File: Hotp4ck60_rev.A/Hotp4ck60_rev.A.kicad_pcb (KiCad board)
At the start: 2 copper layers, 284.7 x 94.2 mm, 43 parts, among them Q1 2N7002, SW1 PWR, U1 nRF52840, U2 BQ24075RGT, U3 TPS7A20xxxDQN, U4 MAX17048, X1 32 MHz, X2 32.768 KHz

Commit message: 기판 아트웍 재시작
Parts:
- removed the REF** at (0.00, 0.00)
- added REF**: hotp4ck60, lib:Neo60-2, F.Cu at (0.00, 0.00)
- C1, C10, C11, C12, C13, C14, C15, C16, C2, C21, C22, C23, C3, C4, C5, C6, C7, C8, C9, L1, L2, R6, R7, U1, U3, U4, X1, X2: moved to B.Cu
- U2: footprint Package_DFN_QFN:VQFN-16-1EP_3x3mm_P0.5mm_EP1.6x1.6mm -> lib:VQFN-16-1EP_3x3mm_P0.5mm_EP1.6x1.6mm; moved to B.Cu
- moved U2 144.5 mm to (-38.1, -27.4), turned to 180 degrees
- moved R6 85.6 mm to (7.24, 23.0), turned to 180 degrees
- moved R7 85.6 mm to (7.24, 25.0), turned to 180 degrees
- moved L2 80.9 mm to (-4.92, 35.4), turned to -90 degrees
- moved X2 79.5 mm to (0.38, 31.8)
- moved U3 77.4 mm to (7.54, 30.9)
- moved U1 74.4 mm to (2.13, 37.4), turned to -90 degrees
- moved L1 74.0 mm to (-3.85, 33.7), turned to 180 degrees
- moved X1 72.4 mm to (-3.74, 41.6), turned to -90 degrees
- moved C6 69.7 mm to (-2.66, 32.0), turned to -90 degrees
- moved C22 69.5 mm to (5.08, 31.0)
- moved C21 67.7 mm to (7.20, 29.4), turned to 180 degrees
- moved C16 65.8 mm to (1.08, 29.8), turned to 90 degrees
- moved C13 65.3 mm to (-5.56, 40.6), turned to -90 degrees
- moved C14 65.3 mm to (-5.56, 42.6), turned to 90 degrees
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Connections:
- U1 pad AC13: unconnected-(U1-P0.18/~{RESET}-PadAC13) -> /~{RST}
- U1 pad AD12: unconnected-(U1-P0.17-PadAD12) -> /~{RST}
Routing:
- net VDD: track 0.00 -> 52.4 mm, vias 0 -> 5
- net GND: track 0.00 -> 16.4 mm, vias 0 -> 14
- net /DEC4_6: track 0.00 -> 15.0 mm, vias 0 -> 2
- net /XC1: track 0.00 -> 5.94 mm
- net /XC2: track 0.00 -> 5.07 mm
- net /XL2: track 0.00 -> 4.72 mm
- net /XL1: track 0.00 -> 4.72 mm
- net /DECUSB: track 0.00 -> 4.24 mm
- net VBUS: track 0.00 -> 4.13 mm
- net /~{RST}: track 0.00 -> 3.83 mm
- net unconnected-(U1-P0.13-PadAD8): track 0.00 -> 3.31 mm
- net unconnected-(U1-D--PadAD4): track 0.00 -> 3.30 mm
- net unconnected-(U1-P0.15-PadAD10): track 0.00 -> 3.28 mm
- net unconnected-(U1-D+-PadAD6): track 0.00 -> 3.27 mm
- net /DEC3: track 0.00 -> 3.14 mm
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- added copper zone on B.Cu, net +VSW
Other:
- outline, holes or cut-outs redrawn

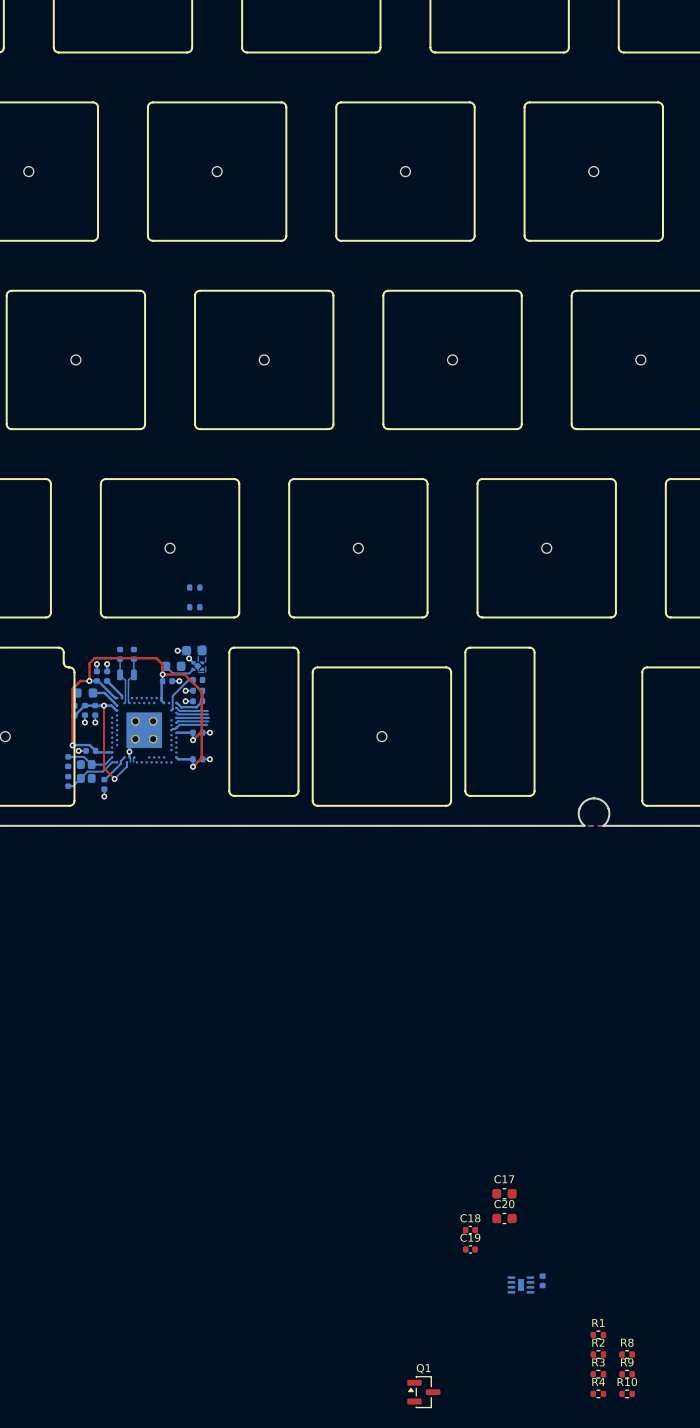
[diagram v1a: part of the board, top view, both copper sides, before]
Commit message: 키보드 기판 소자 재배치 중
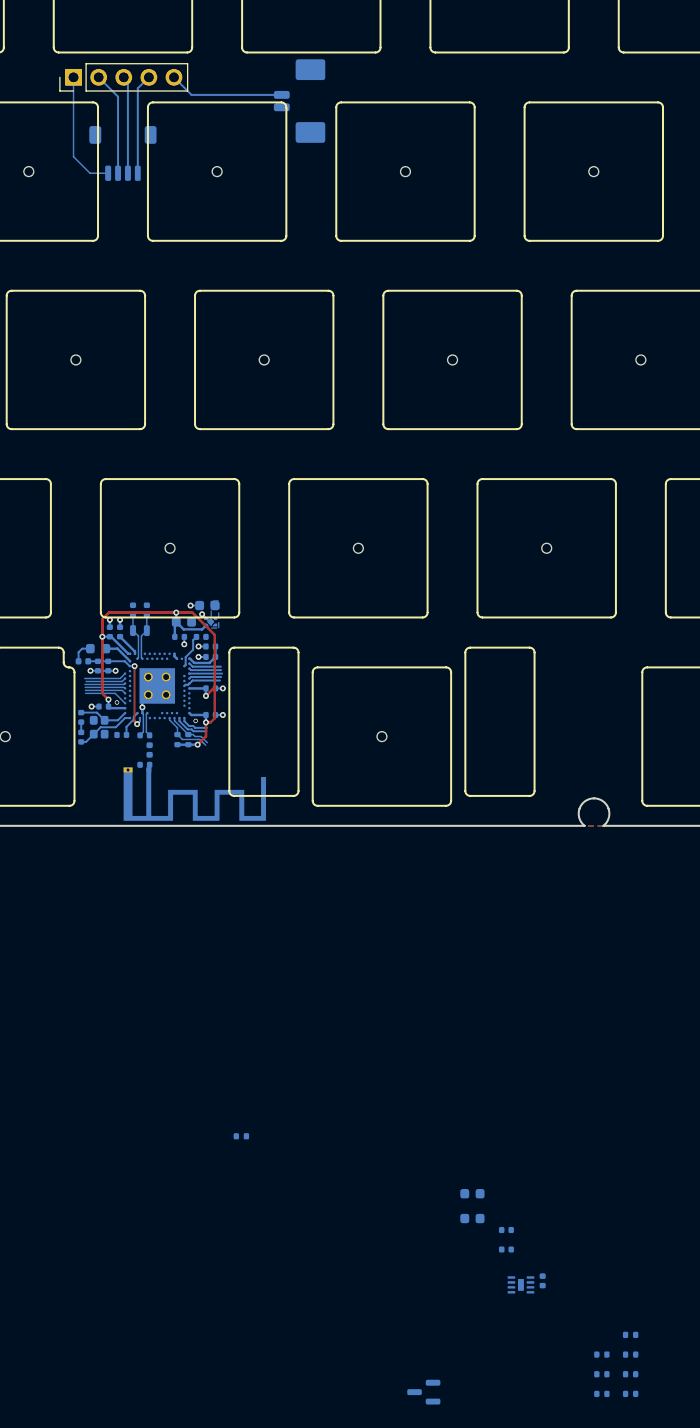
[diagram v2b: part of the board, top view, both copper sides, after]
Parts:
- added AE1: ANT, RF_Antenna:Texas_SWRA117D_2.4GHz_Right, B.Cu at (2.59, 41.5)
- added C24: 0.8nF, Capacitor_SMD:C_0402_1005Metric, B.Cu at (2.19, 38.0)
- added C25: 0.5nF, Capacitor_SMD:C_0402_1005Metric, B.Cu at (2.19, 40.9)
- added J1: POGO, Connector_PinHeader_2.54mm:PinHeader_1x05_P2.54mm_Vertical, F.Cu at (-5.03, -28.6)
- added J2: ai03_unified_daughter_board, Connector_JST:JST_SH_SM04B-SRSS-TB_1x04-1MP_P1.00mm_Horizontal, B.Cu at (-0.03, -20.9)
- added J3: Battery Connector, Connector_Molex:Molex_PicoBlade_53261-0271_1x02-1MP_P1.25mm_Horizontal, B.Cu at (18.4, -26.2)
- added L3: 4.7nH, 700mA, Inductor_SMD:L_0402_1005Metric, B.Cu at (2.67, 39.4)
- added R1: 0Ω, Resistor_SMD:R_0402_1005Metric, B.Cu at (11.9, 78.5)
- C17, C18, C19, C20, Q1, R10, R8, R9: moved to B.Cu
- L1: value 10 uH, 50mA -> 10uH,50mA
- L2: value 15 nH -> 15nH
- R2: renamed from R1; moved to B.Cu
- R3: renamed from R2; moved to B.Cu
- R4: renamed from R3; moved to B.Cu
- R5: renamed from R4; moved to B.Cu
- moved R6 15.4 mm to (6.59, 38.4), turned to 90 degrees
- moved R7 13.5 mm to (5.49, 38.4), turned to 90 degrees
- moved C2 5.30 mm to (-0.15, 37.9), turned to 180 degrees
- moved L2 5.06 mm to (-4.03, 30.5), turned to 0 degrees
- moved C21 4.75 mm to (8.51, 24.8)
- moved C1 4.67 mm to (-0.32, 27.5)
- moved C6 4.67 mm to (-1.35, 27.5)
- moved C7 4.67 mm to (-1.97, 35.0)
- moved C12 4.67 mm to (8.85, 30.0)
- moved C16 4.67 mm to (2.39, 25.3)
- moved C3 4.67 mm to (-1.52, 30.9)
- moved C4 4.67 mm to (-2.56, 30.9)
- moved U3 4.67 mm to (8.85, 26.5)
- moved C10 4.67 mm to (8.85, 35.9)
- moved C11 4.67 mm to (8.85, 29.0)
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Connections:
- Q1 pad 2: Net-(Q1-S) -> GND
- R9 pad 2: Net-(Q1-S) -> GND
- SW1 pad 3: Net-(Q1-S) -> GND
- U1 pad AD4: unconnected-(U1-D--PadAD4) -> /D-
- U1 pad AD6: unconnected-(U1-D+-PadAD6) -> /D+
- U1 pad H23: unconnected-(U1-ANT-PadH23) -> Net-(U1-ANT)
- U1 pad U24: unconnected-(U1-P1.04-PadU24) -> /SCL
- U1 pad W24: unconnected-(U1-P1.02-PadW24) -> /SDA
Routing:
- net /D-: track 0.00 -> 13.8 mm
- net GND: track 16.4 -> 29.8 mm, vias 14 -> 15
- net /D+: track 0.00 -> 13.1 mm
- net VBUS: track 4.13 -> 16.3 mm
- net +BATT: track 0.00 -> 11.6 mm
- net /SCL: track 0.00 -> 5.30 mm
- net /SDA: track 0.00 -> 4.51 mm
- net unconnected-(U1-P1.10-PadA20): track 0.00 -> 4.40 mm
- net unconnected-(U1-AIN7/P0.31-PadA8): track 0.00 -> 4.28 mm
- net unconnected-(U1-P1.13-PadA16): track 0.00 -> 4.14 mm
- net unconnected-(U1-AIN0/P0.02-PadA12): track 0.00 -> 4.10 mm
- net unconnected-(U1-P1.15-PadA14): track 0.00 -> 4.08 mm
- net unconnected-(U1-AIN5/P0.29-PadA10): track 0.00 -> 4.07 mm
- net unconnected-(U1-SWDCLK-PadAA24): track 0.00 -> 3.48 mm
- net unconnected-(U1-D--PadAD4): track 3.30 -> 0.00 mm
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
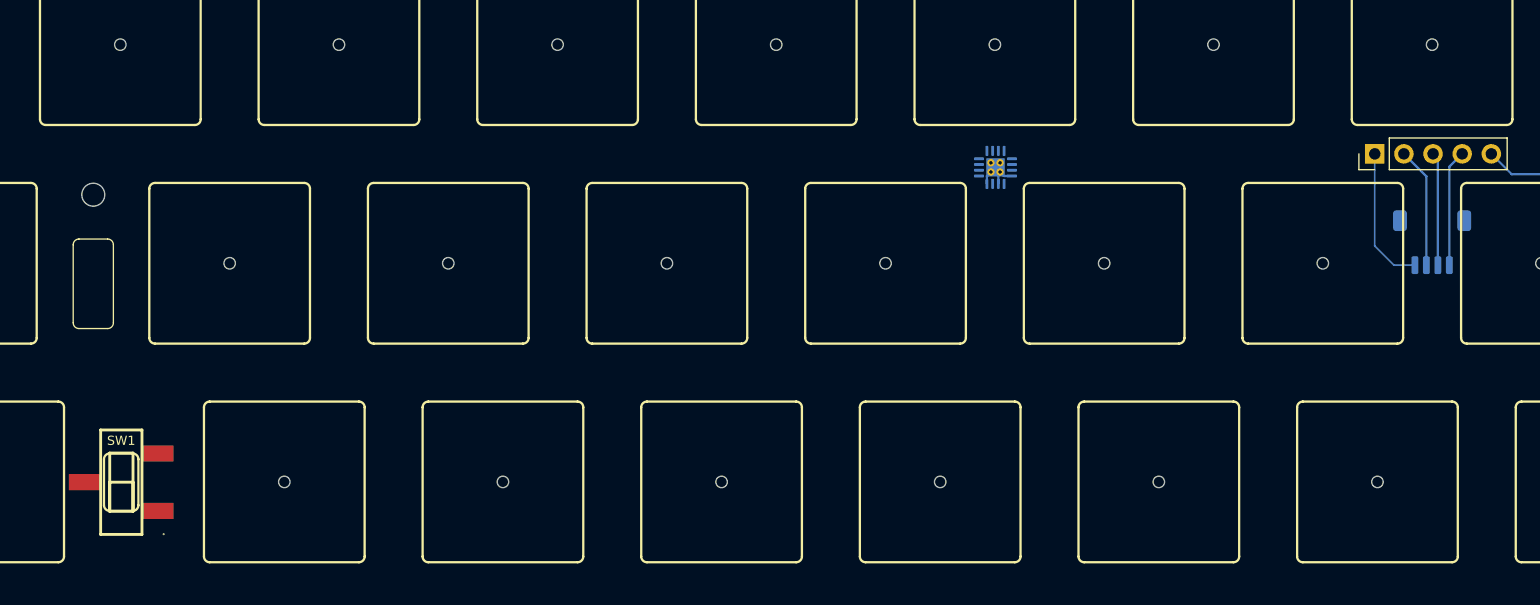
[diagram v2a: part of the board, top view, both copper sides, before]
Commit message: 키보드 기판 소자 재배치 중
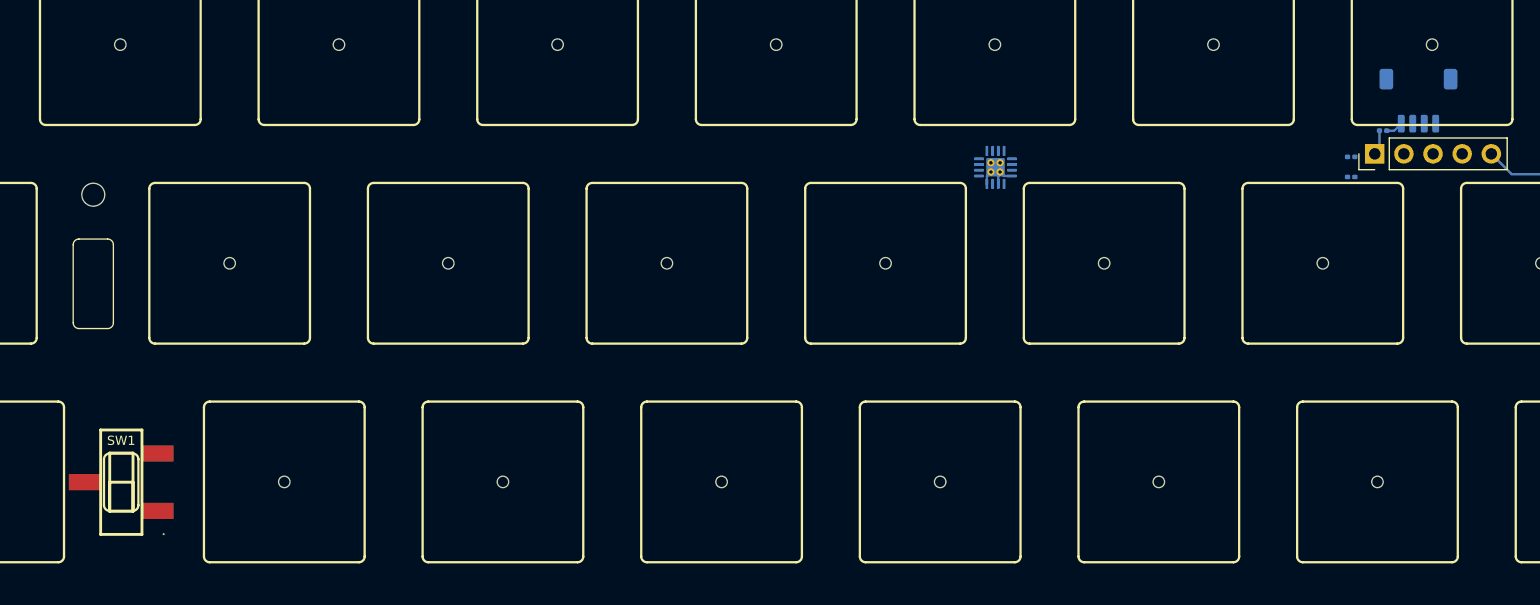
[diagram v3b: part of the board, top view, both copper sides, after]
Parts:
- added JP1: 0Ω, Resistor_SMD:R_0201_0603Metric, B.Cu at (-4.29, -30.6)
- added JP2: 0Ω, Resistor_SMD:R_0201_0603Metric, B.Cu at (-7.08, -28.3)
- added JP3: 0Ω, Resistor_SMD:R_0201_0603Metric, B.Cu at (-7.08, -26.6)
- moved J2 12.4 mm to (-1.22, -33.2)
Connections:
- J2 pad 1: VBUS -> Net-(J2-Pin_1)
- J2 pad 2: /D- -> Net-(J2-Pin_2)
- J2 pad 3: /D+ -> Net-(J2-Pin_3)
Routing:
- net /D-: track 13.8 -> 3.30 mm
- net GND: track 29.8 -> 19.7 mm
- net /D+: track 13.1 -> 3.27 mm
- net VBUS: track 16.3 -> 6.64 mm
- net Net-(J2-Pin_1): track 0.00 -> 1.51 mm
